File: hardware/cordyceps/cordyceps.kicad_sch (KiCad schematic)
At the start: 23 parts, among them J1 KH-1.27PH180-2X5P-L7.2-SMT, SW1 TS-1187A-B-A-B, U1 nRF52833-QDxx, X1 32Mhz crystal, X2 32.768kHz crystal

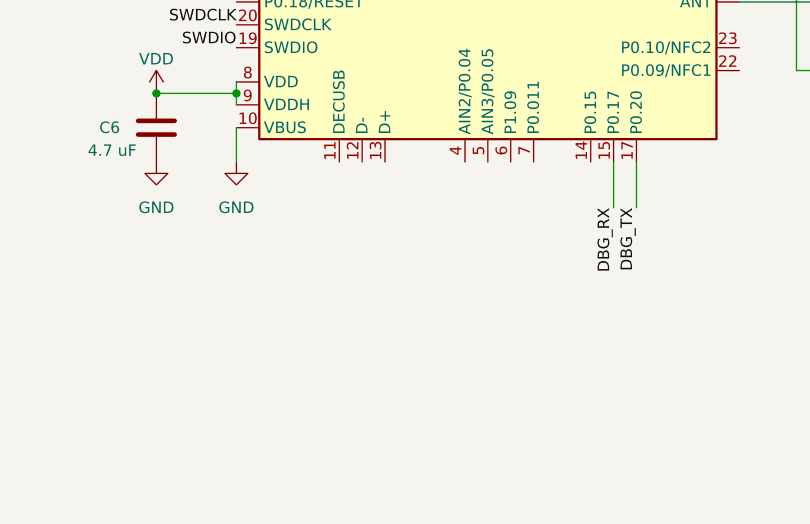
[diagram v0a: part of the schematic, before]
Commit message: Add 2 MOSFETs to be able to turn things on and off
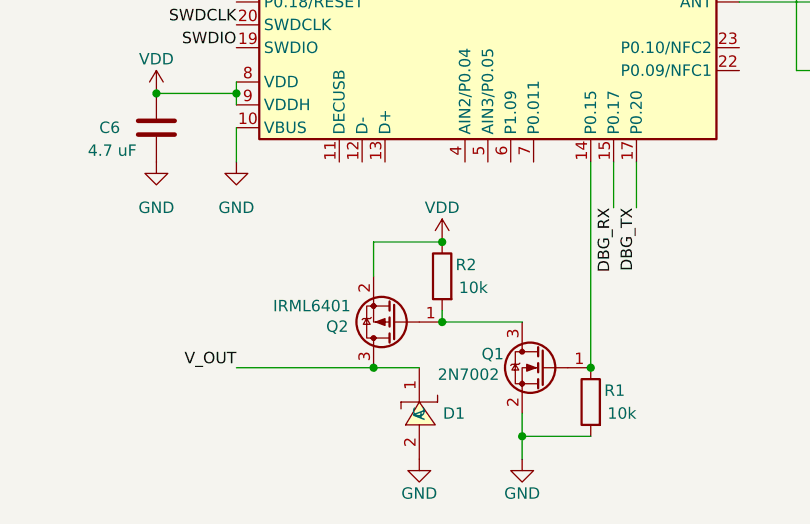
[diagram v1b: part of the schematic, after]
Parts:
- added D1: 1N5819WS, easyeda2kicad:SOD-323_L1.8-W1.3-LS2.5-RD, symbol easyeda2kicad:1N5819WS
- added Q1: 2N7002, Package_TO_SOT_SMD:SOT-23, symbol Ostranna:2N7002
- added Q2: IRML6401, Package_TO_SOT_SMD:SOT-23, symbol Ostranna:IRML6401
- added R1, R2: 10k, Resistor_SMD:R_0402_1005Metric, symbol Ostranna:10k Resistor
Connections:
- net GND: now also D1.2 (A), Q1.2 (S), R1.2
- net VDD: now also Q2.2 (S), R2.1
- net at U1.14 (P0.15): now also Q1.1 (G), R1.1
- new net: Q1.3 (D), Q2.1 (G), R2.2
- new net V_OUT: D1.1 (C), Q2.3 (D)

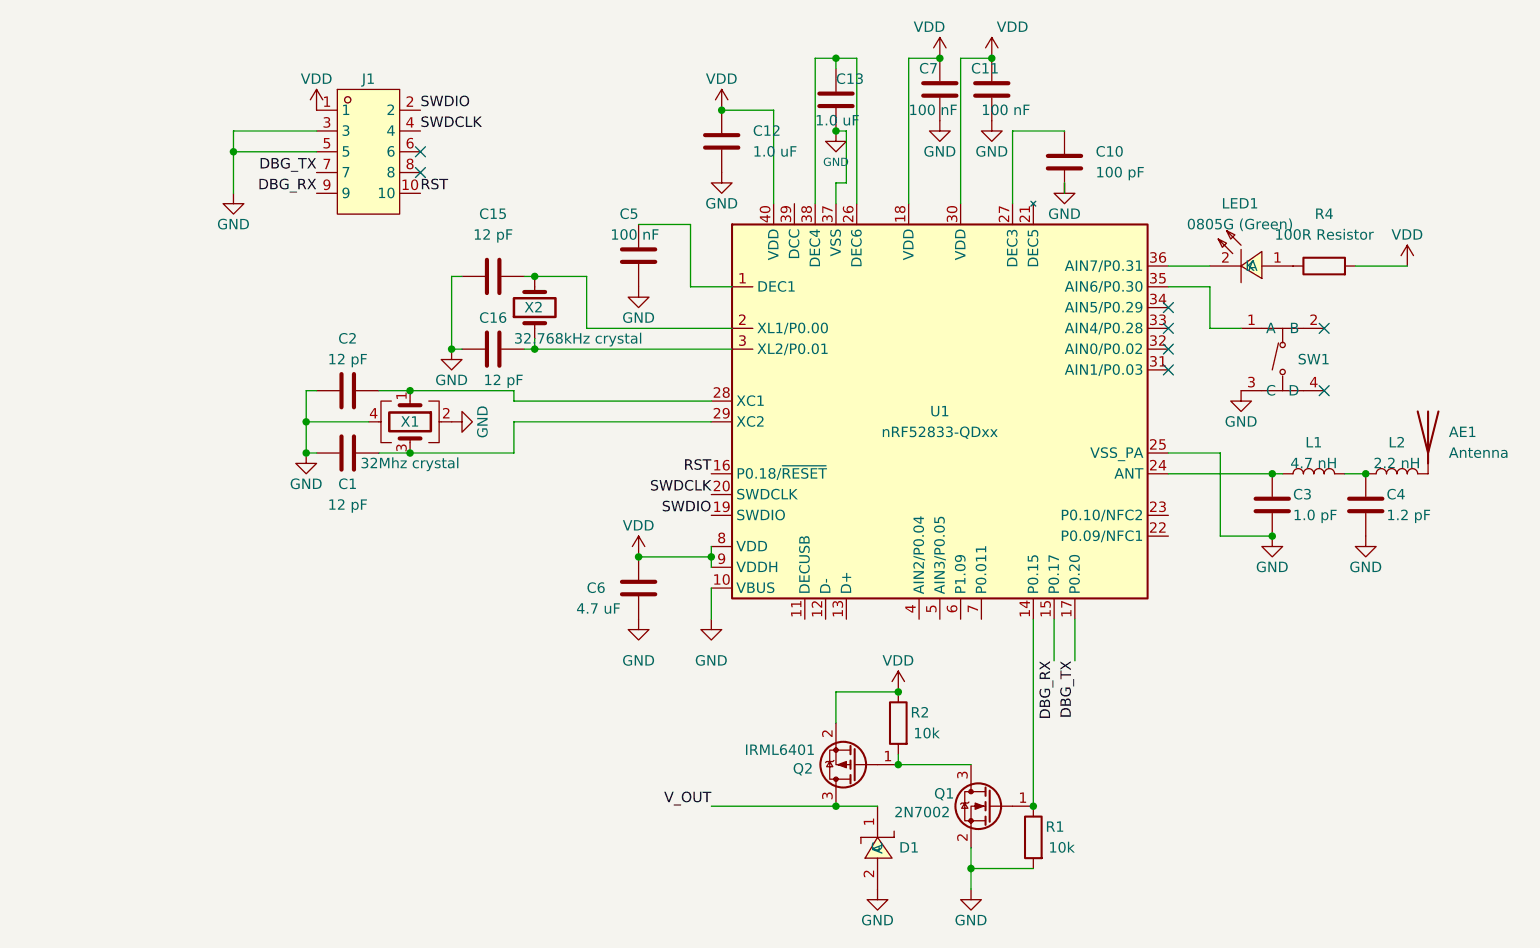
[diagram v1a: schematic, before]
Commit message: Add required connectors
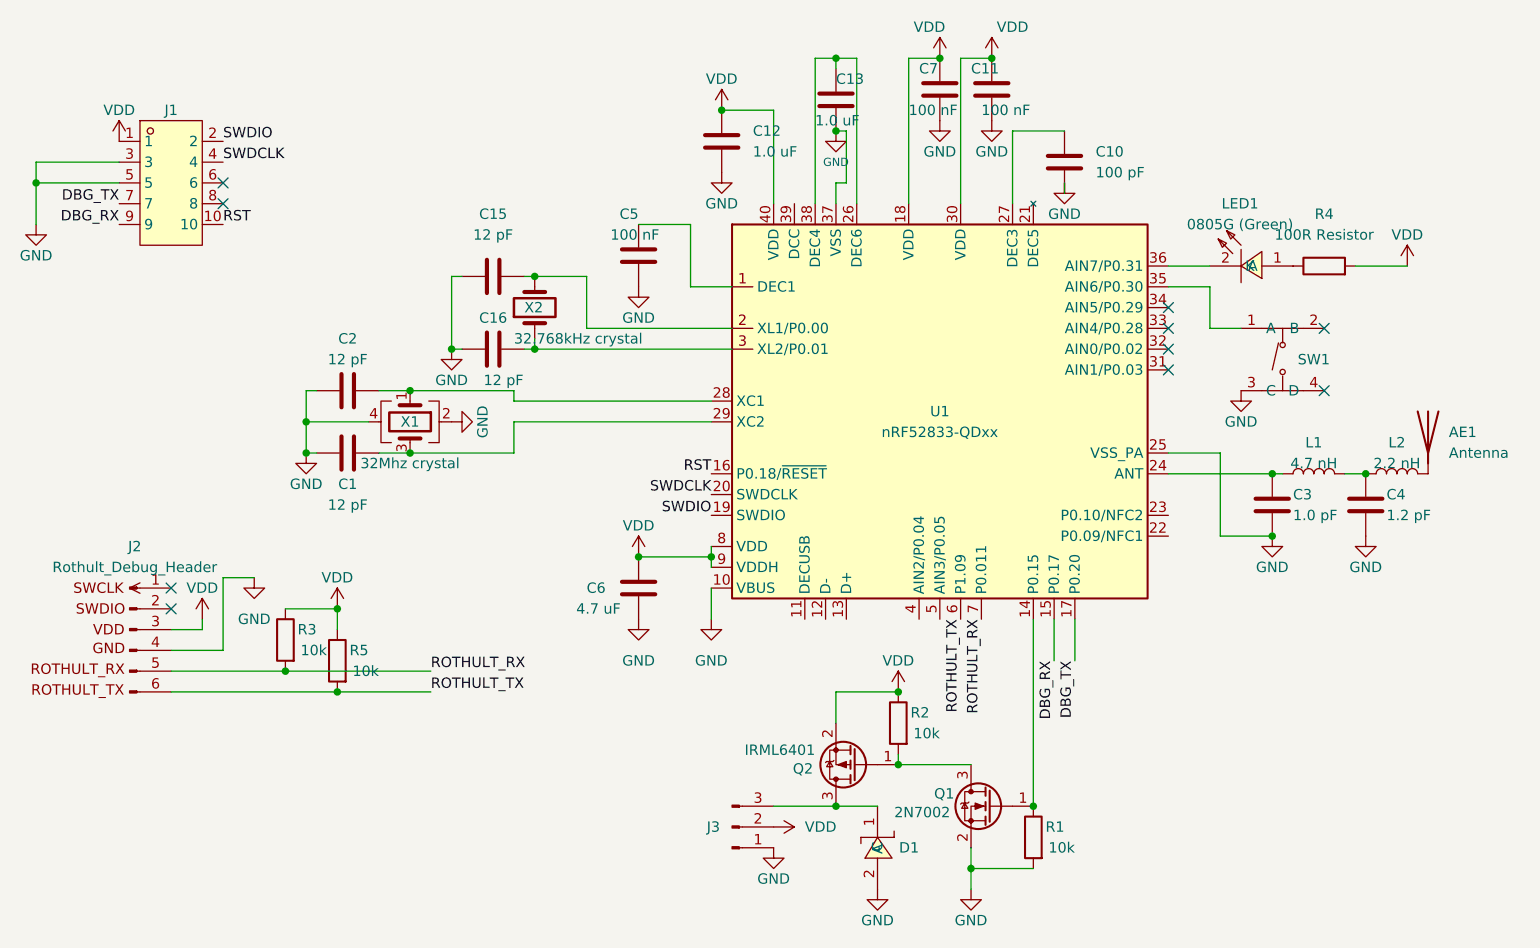
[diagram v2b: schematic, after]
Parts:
- added J2: Rothult_Debug_Header, Connector_PinHeader_1.27mm:PinHeader_1x06_P1.27mm_Vertical, symbol Common:Rothult_Debug_Header
- added J3: Conn_01x03_Pin, Connector_PinHeader_2.54mm:PinHeader_1x03_P2.54mm_Vertical, symbol Connector:Conn_01x03_Pin
- added R3, R5: 10k, Resistor_SMD:R_0402_1005Metric, symbol Ostranna:10k Resistor
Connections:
- net GND: now also J2.4 (GND), J3.1 (Pin_1)
- net VDD: now also J2.3 (VDD), J3.2 (Pin_2), R3.1, R5.1
- net ROTHULT_TX: now reaches U1.6 (P1.09)
- net ROTHULT_TX: now also J2.6 (ROTHULT_TX), R5.2
- net ROTHULT_RX: now reaches U1.7 (P0.011)
- net ROTHULT_RX: now also J2.5 (ROTHULT_RX), R3.2
- net V_OUT: no longer names the net of D1.1 (C), Q2.3 (D)
- net V_OUT: now also J3.3 (Pin_3)
- no-connect marks 8 -> 10
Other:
- moved on the sheet: J1

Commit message: Fix the small fuckup with the UART RX/TX on cordyceps board
Oops, I did it again!
Luckily, we can just reassign those as nRF chips allow to use any pin as RX/TX.
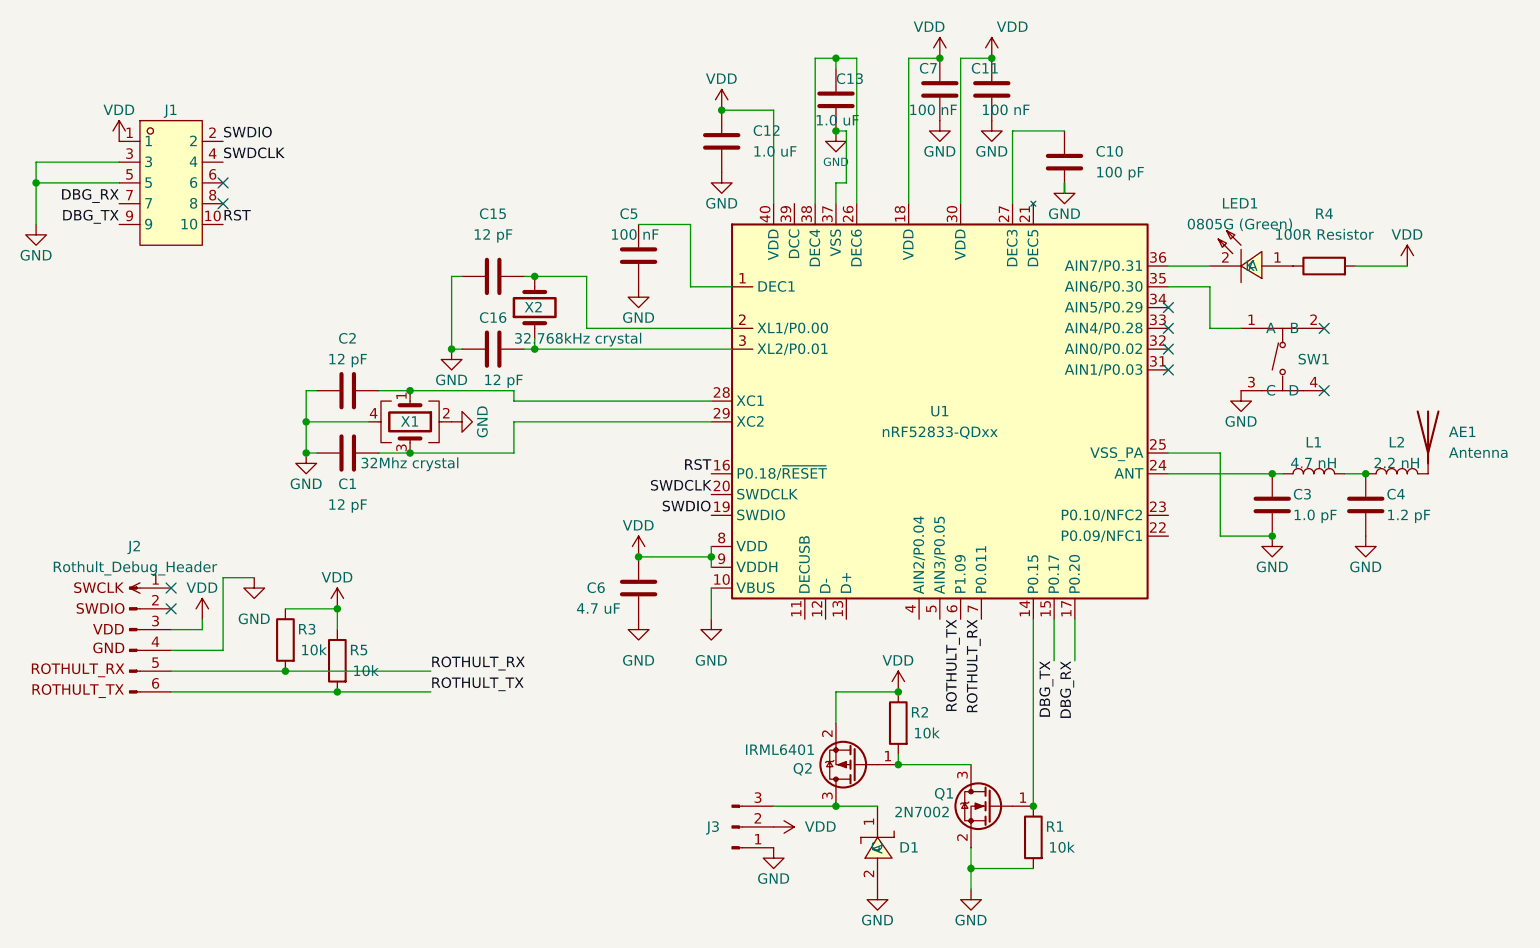
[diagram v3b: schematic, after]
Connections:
- net DBG_RX: now also J1.7, U1.17 (P0.20); no longer J1.9, U1.15 (P0.17)
- net DBG_TX: now also J1.9, U1.15 (P0.17); no longer J1.7, U1.17 (P0.20)
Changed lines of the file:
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@@
 		)
 	)
-	(label "DBG_TX"
+	(label "DBG_RX"
 		(at 191.77 125.73 270)
 		(fields_autoplaced yes)
@@
 		)
 	)
-	(label "DBG_TX"
+	(label "DBG_RX"
 		(at 74.93 69.85 180)
 		(fields_autoplaced yes)
@@
 		)
 	)
-	(label "DBG_RX"
+	(label "DBG_TX"
 		(at 189.23 125.73 270)
 		(fields_autoplaced yes)
@@
 		)
 	)
-	(label "DBG_RX"
+	(label "DBG_TX"
 		(at 74.93 72.39 180)
 		(fields_autoplaced yes)
